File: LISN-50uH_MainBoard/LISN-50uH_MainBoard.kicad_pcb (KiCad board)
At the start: 2 copper layers, 160 x 120 mm, 80 parts, among them J1 Faston Tab 4.8mm, J2 Faston Tab 4.8mm, J3 Faston Tab 4.8mm, J4 Faston Tab 4.8mm, J5 Conn_Coaxial, J6 Conn_Coaxial, J7 Faston Tab 4.8mm, J8 Faston Tab 4.8mm

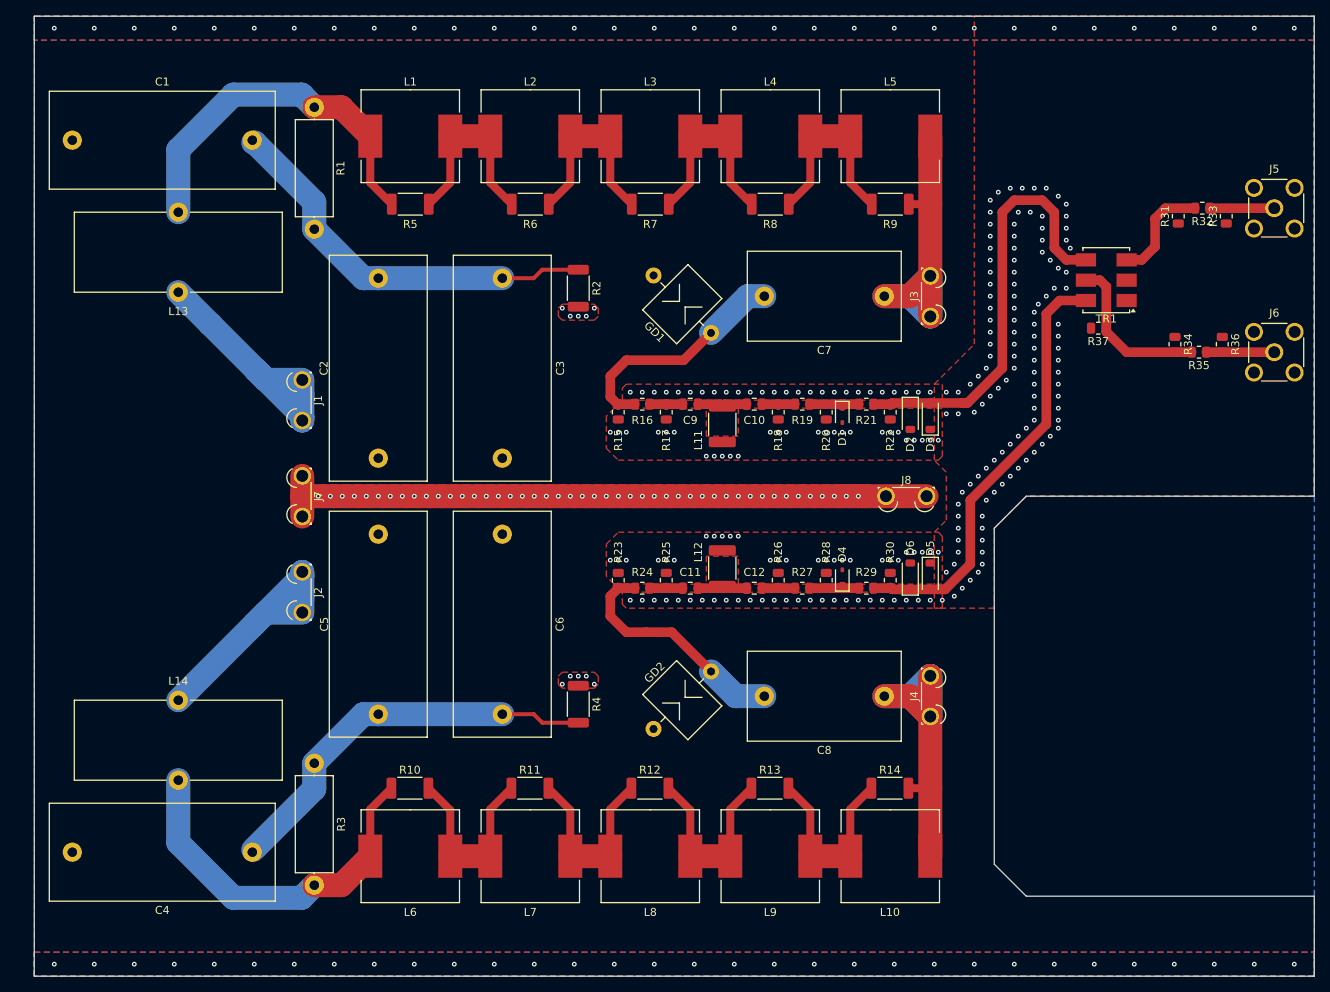
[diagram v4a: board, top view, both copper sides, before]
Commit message: add L&N/CM&DM switch
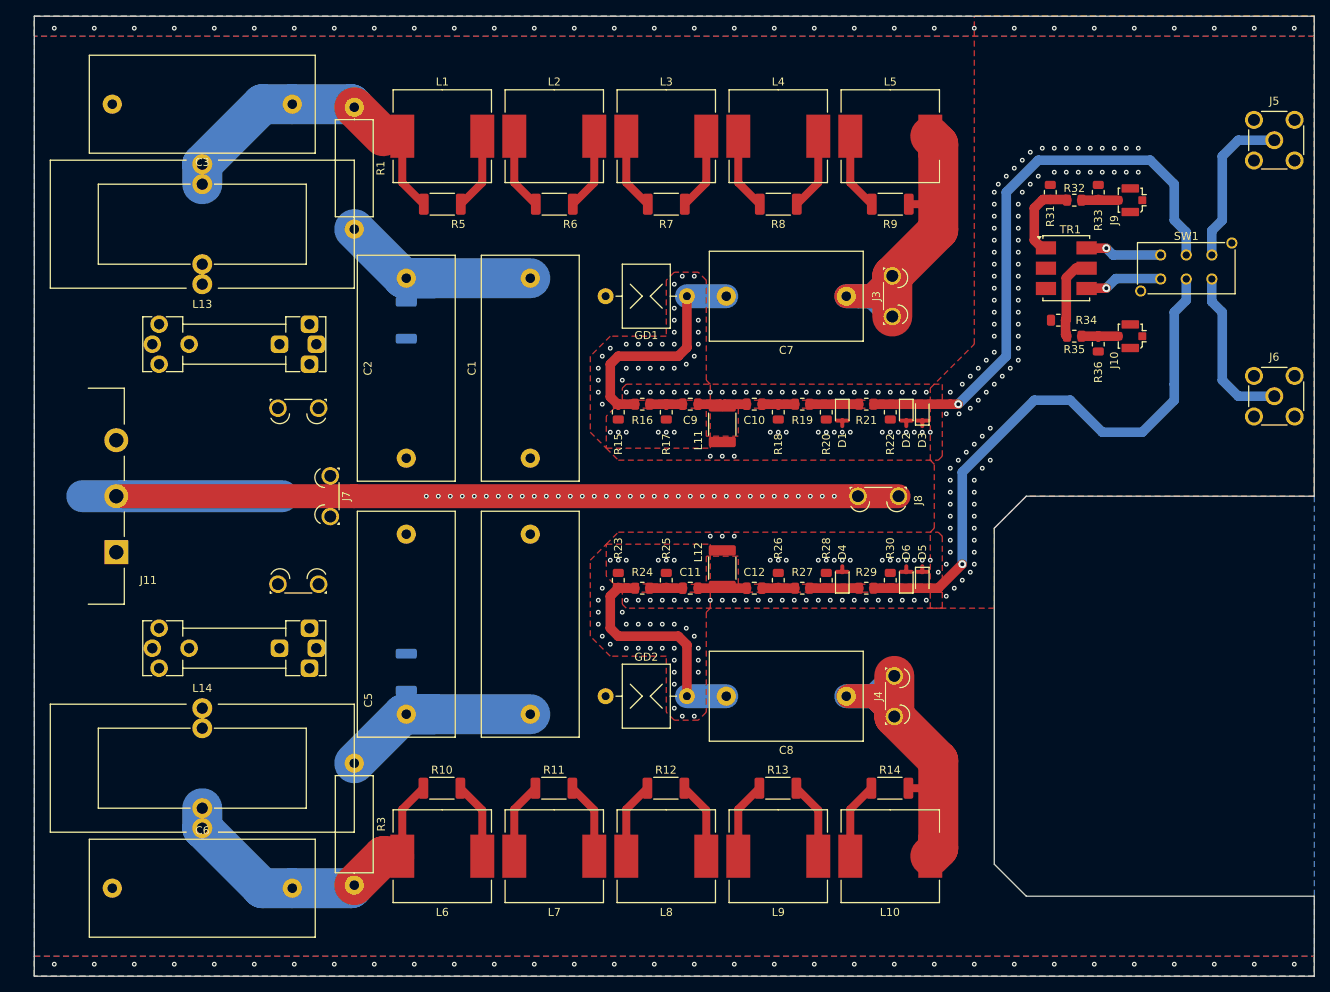
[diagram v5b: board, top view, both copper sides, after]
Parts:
- removed R37: 50R, Resistor_SMD:R_0805_2012Metric
- added F1: 10A, a_project_library:Fuseholder_Clip-5x20mm_Littelfuse_100_111_dual_Horizontal, F.Cu at (95.0, 81.0)
- added F2: 10A, a_project_library:Fuseholder_Clip-5x20mm_Littelfuse_100_111_dual_Horizontal, F.Cu at (95.0, 119.0)
- added J10: Conn_Coaxial, Connector_Coaxial:U.FL_Molex_MCRF_73412-0110_Vertical, F.Cu at (207.0, 80.0)
- added J11: Conn_01x03_Pin, a_project_library:AC_Connector_Adam_tech_IEC-A-4, F.Cu at (80.2, 107.0)
- added J9: Conn_Coaxial, Connector_Coaxial:U.FL_Molex_MCRF_73412-0110_Vertical, F.Cu at (207.0, 63.0)
- added SW1: SW_DPDT_x2, a_project_library:SW_E-SWITCH_LC2255EENP_DPDT_right_angle, F.Cu at (214.0, 71.5)
- D2, D3, D5, D6: value 1N4150 -> BAS321,115; footprint Diode_SMD:D_SOD-123 -> Diode_SMD:D_SOD-323
- L13, L14: footprint a_project_library:L_Toroid_Vertical_L26.0mm_W12.9mm_P10.0mm_Wuerth_WE-FI -> a_project_library:L_Toroid_Vertical_L38.0mm_W16.0mm_P15.0mm_Wuerth_WE-FI
- R2, R4: value R -> 470k; moved to B.Cu
- moved C1 38.8 mm to (132.0, 72.8), turned to -90 degrees
- moved C4 38.8 mm to (132.0, 127.2), turned to 90 degrees
- moved C3 34.1 mm to (102.2, 51.0), turned to 180 degrees
- moved C6 34.1 mm to (102.2, 149.0), turned to 180 degrees
- moved R2 21.9 mm to (116.5, 78.0)
- moved R4 21.9 mm to (116.5, 122.0)
- moved R31 16.3 mm to (197.0, 62.0), turned to -90 degrees
- moved R33 16.3 mm to (203.0, 62.0), turned to -90 degrees
- moved R32 16.0 mm to (200.0, 63.0)
- moved R35 15.7 mm to (200.0, 80.0)
- moved R36 15.5 mm to (203.0, 81.0), turned to 90 degrees
- moved R34 14.9 mm to (198.0, 78.0), turned to 0 degrees
- moved J5 8.50 mm to (225.0, 55.5)
- moved J6 5.50 mm to (225.0, 87.5)
- moved TR1 5.22 mm to (199.0, 71.5), turned to 0 degrees
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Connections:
- C1 pad 1: /L_C -> /L_Cap
- C2 pad 1: /L_C -> /L_Cap
- C3 pad 1: /L_C -> /L_l
- C4 pad 1: /N_C -> /N_Cap
- C5 pad 1: /N_C -> /N_Cap
- C6 pad 1: /N_C -> /N_l
- J5 pad 1: /SIG_DM_out -> Net-(J5-In)
- J6 pad 1: /SIG_CM_out -> Net-(J6-In)
- L13 pad 1: /L_in -> /L_fused
- L14 pad 1: /N_in -> /N_fused
- R1 pad 1: /L_C -> /L_Cap
- R2 pad 2: /L_C -> /L_Cap
- R3 pad 1: /N_C -> /N_Cap
- R4 pad 2: /N_C -> /N_Cap
- TR1 pad 1: GND -> /SIG_DM
- TR1 pad 3: /SIG_DM -> GND
- TR1 pad 4: L_SIG_LIM -> Net-(SW1B-C)
- TR1 pad 6: N_SIG_LIM -> Net-(SW1A-A)
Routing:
- net GND: track 82.1 -> 134.6 mm, vias 344 -> 350
- net /L_C: track 50.1 -> 0.00 mm
- net /N_C: track 50.0 -> 0.00 mm
- net /L_in: track 34.8 -> 0.00 mm
- net /N_in: track 34.6 -> 0.00 mm
- net /N_Cap: track 0.00 -> 31.0 mm
- net /L_Cap: track 0.00 -> 31.0 mm
- net Net-(J6-In): track 0.00 -> 20.5 mm
- net Net-(J5-In): track 0.00 -> 20.2 mm
- net N_SIG_LIM: track 54.4 -> 73.1 mm, vias 0 -> 1
- net L_SIG_LIM: track 54.3 -> 72.9 mm, vias 0 -> 1
- net /SIG_CM: track 20.3 -> 10.4 mm
- net Net-(SW1B-C): track 0.00 -> 9.80 mm, vias 0 -> 1
- net Net-(SW1A-A): track 0.00 -> 9.63 mm, vias 0 -> 1
- net /L_l: track 46.4 -> 39.5 mm
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
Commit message: Planes added
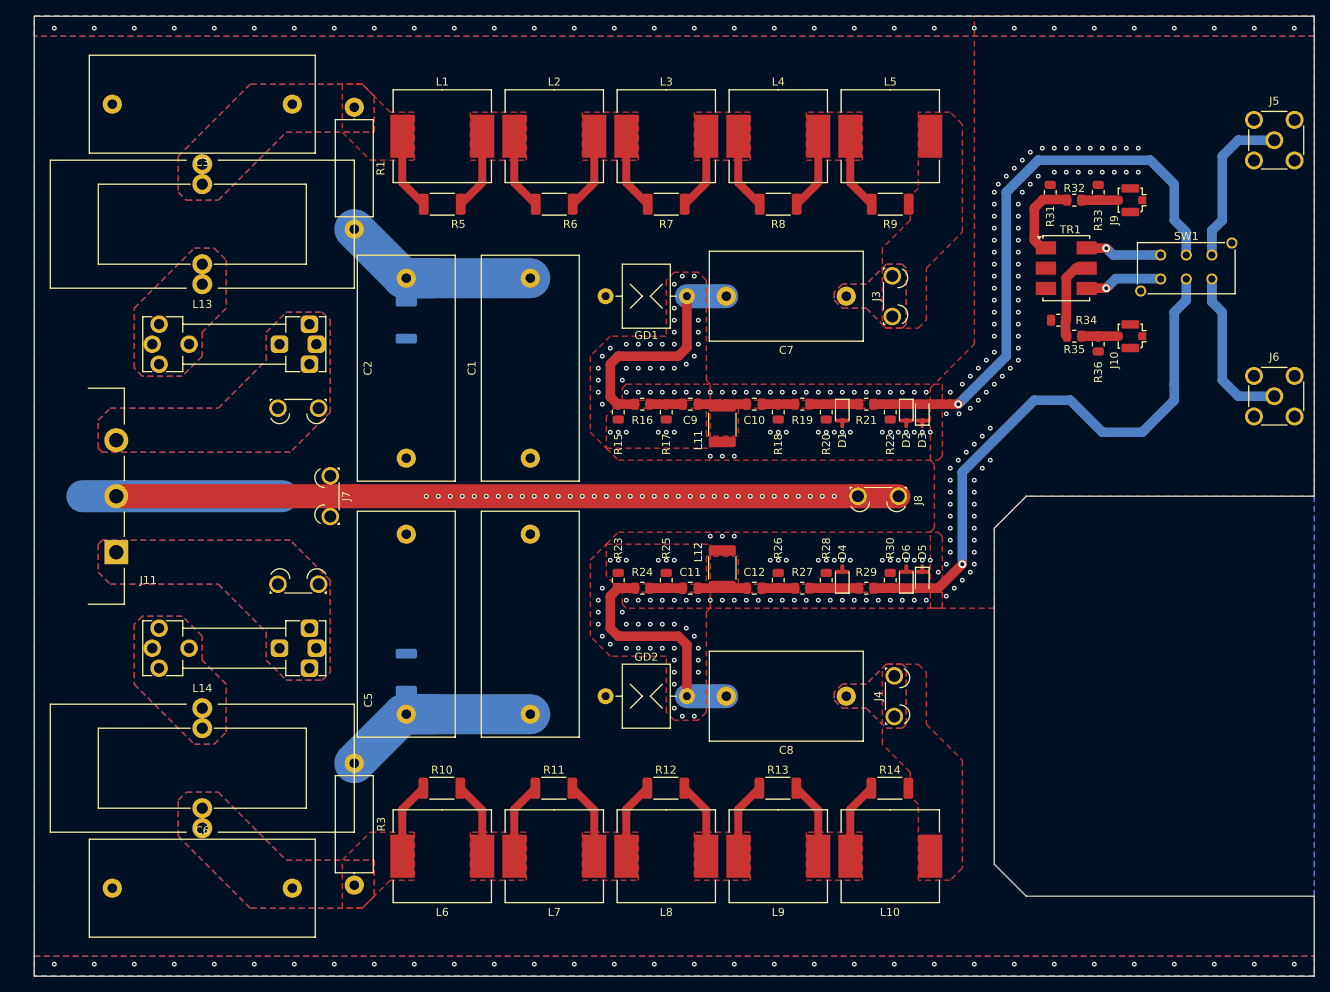
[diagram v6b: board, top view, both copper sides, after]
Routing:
- net /L_dut: track 54.4 -> 0.00 mm
- net /N_dut: track 52.8 -> 0.00 mm
- net /N_l: track 40.9 -> 9.59 mm
- net /L_l: track 39.5 -> 9.61 mm
- added copper zone on B.Cu, net /L_dut
- added copper zone on F.Cu, net /L_dut
- added copper zone on B.Cu, net /L_fused
- added copper zone on F.Cu, net /L_fused
- added copper zone on B.Cu, net /L_in
- added copper zone on F.Cu, net /L_in
- added copper zone on B.Cu, net /L_l
- added copper zone on F.Cu, net /L_l
- added copper zone on F.Cu, net /L_l1
- added copper zone on F.Cu, net /L_l2
- added copper zone on F.Cu, net /L_l3
- added copper zone on F.Cu, net /L_l4
- added copper zone on B.Cu, net /N_dut
- added copper zone on F.Cu, net /N_dut
- added copper zone on B.Cu, net /N_fused
- added copper zone on F.Cu, net /N_fused
- added copper zone on B.Cu, net /N_in
- added copper zone on F.Cu, net /N_in
- added copper zone on B.Cu, net /N_l
- added copper zone on F.Cu, net /N_l
- added copper zone on F.Cu, net /N_l1
- added copper zone on F.Cu, net /N_l2
- added copper zone on F.Cu, net /N_l3
- added copper zone on F.Cu, net /N_l4

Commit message: add RF track via shielding
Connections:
- SW1 pad 7: (no net) -> GND
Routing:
- net GND: vias 350 -> 509

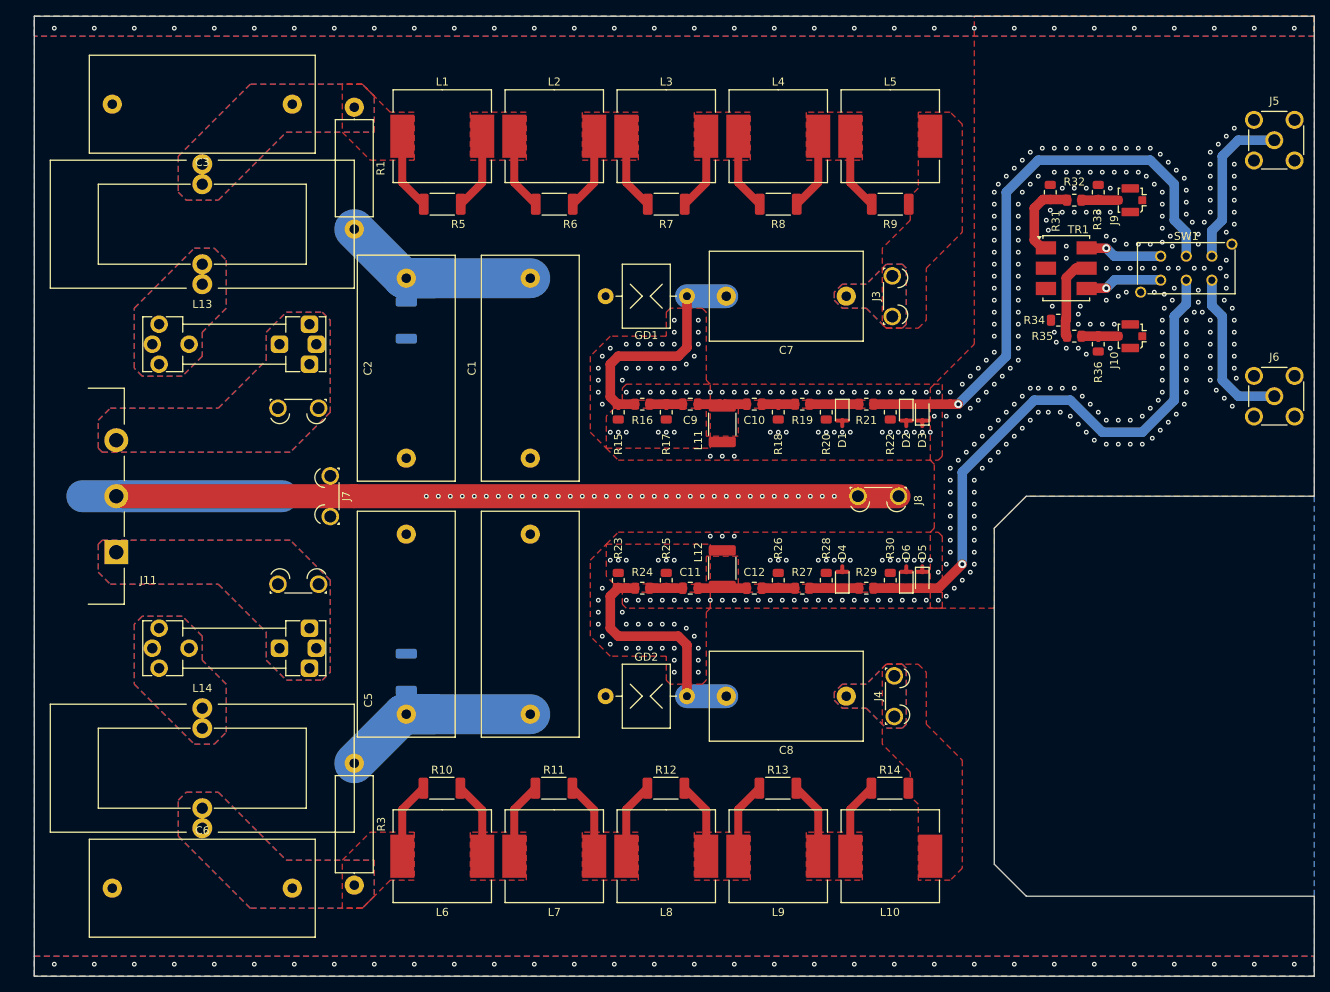
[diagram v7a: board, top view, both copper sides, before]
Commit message: move CM DM to dedicated PCB
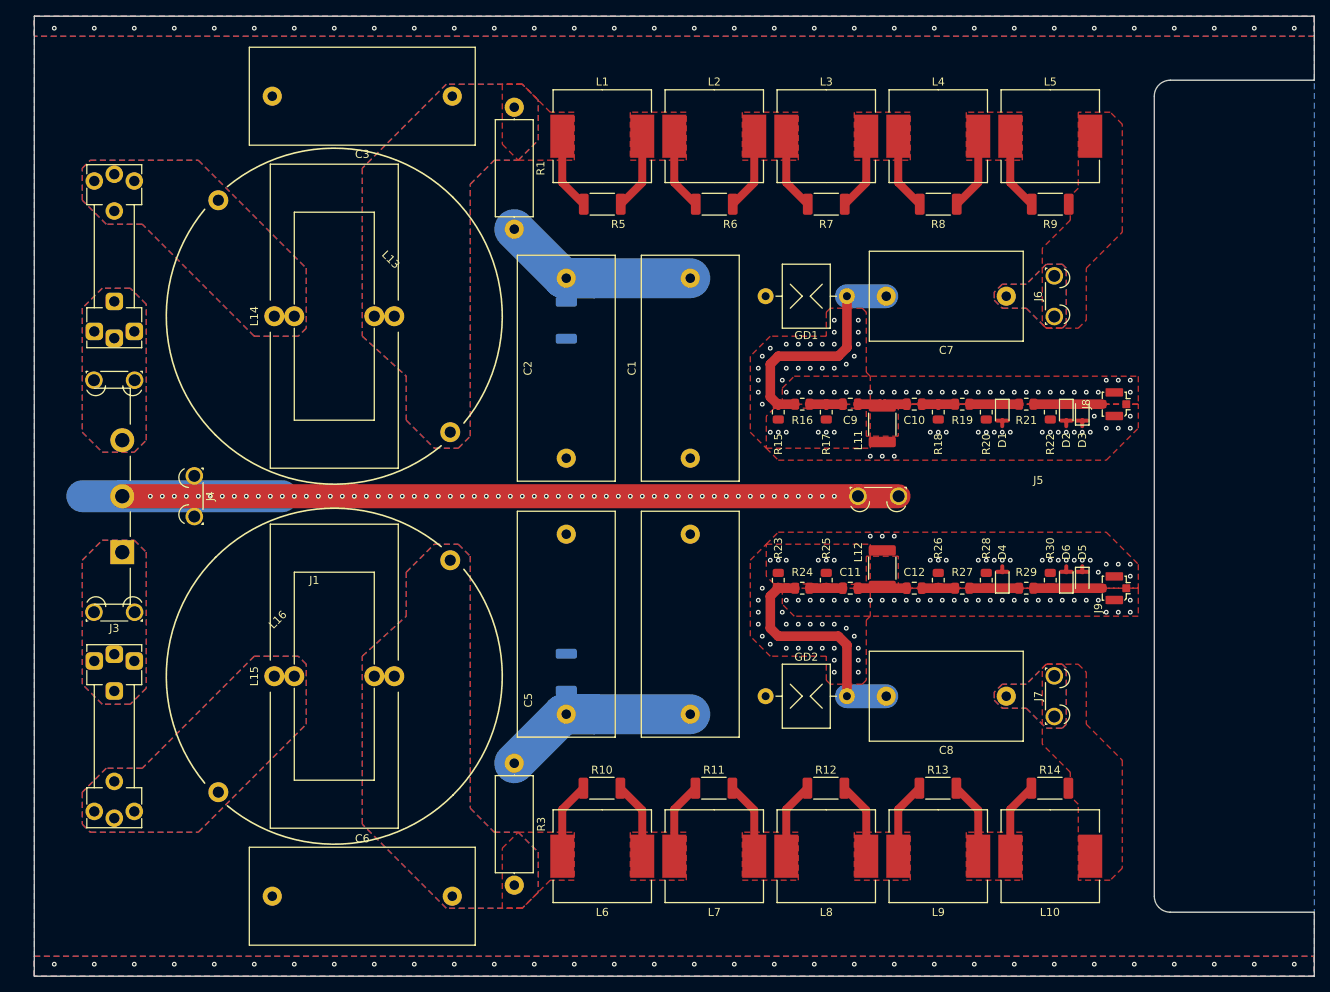
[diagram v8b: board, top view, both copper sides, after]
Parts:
- removed J10: Conn_Coaxial, Connector_Coaxial:U.FL_Molex_MCRF_73412-0110_Vertical
- removed J11: Conn_01x03_Pin, a_project_library:AC_Connector_Adam_tech_IEC-A-4
- removed R31, R33, R34, R36: DNP, Resistor_SMD:R_0805_2012Metric
- removed R32: 0, Resistor_SMD:R_0805_2012Metric
- removed R35: 0R, Resistor_SMD:R_0805_2012Metric
- removed SW1: SW_DPDT_x2, a_project_library:SW_E-SWITCH_LC2255EENP_DPDT_right_angle
- removed TR1: ADT1-6T, RF_Mini-Circuits:Mini-Circuits_CD637_H5.23mm
- added L15: 250uH optional, a_project_library:L_Toroid_Vertical_L38.0mm_W16.0mm_P15.0mm_Wuerth_WE-FI, F.Cu at (107.5, 122.5)
- added L16: 250uH optional, a_project_library:L_Toroid_Horizontal_D42.0mm_H21.5mm_Abracon_ATCA-08, F.Cu at (107.5, 122.5)
- J1: value Faston Tab 4.8mm -> Conn_01x03_Pin; footprint a_project_library:Faston_Tab_4.8x0.8 -> a_project_library:AC_Connector_Adam_tech_IEC-A-4
- J5, J6: value Conn_Coaxial -> Faston Tab 4.8mm; footprint Connector_Coaxial:SMA_Molex_73251-2200_Horizontal -> a_project_library:Faston_Tab_4.8x0.8
- J8: value Faston Tab 4.8mm -> Conn_Coaxial; footprint a_project_library:Faston_Tab_4.8x0.8 -> Connector_Coaxial:U.FL_Molex_MCRF_73412-0110_Vertical
- L13: footprint a_project_library:L_Toroid_Vertical_L38.0mm_W16.0mm_P15.0mm_Wuerth_WE-FI -> a_project_library:L_Toroid_Horizontal_D42.0mm_H21.5mm_Abracon_ATCA-08
- moved J3 105.0 mm to (80.0, 114.5), turned to 0 degrees
- moved J7 93.9 mm to (197.5, 125.0), turned to -90 degrees
- moved J4 91.0 mm to (90.0, 100.0), turned to 90 degrees
- moved J5 66.6 mm to (175.5, 100.0), turned to 180 degrees
- moved L14 58.9 mm to (107.5, 77.5), turned to 90 degrees
- moved J9 48.5 mm to (205.0, 111.5)
- moved J2 34.3 mm to (80.0, 85.5), turned to 180 degrees
- moved J8 31.7 mm to (205.0, 88.5), turned to -90 degrees
- moved J6 30.2 mm to (197.5, 75.0)
- moved J1 28.4 mm to (81.0, 107.0)
- moved L13 20.1 mm to (107.5, 77.5), turned to -45 degrees
- moved C3 20.0 mm to (122.2, 50.0)
- moved C6 20.0 mm to (122.2, 150.0)
- moved C1 20.0 mm to (152.0, 72.8)
- moved C10 20.0 mm to (180.0, 88.5)
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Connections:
- D2 pad 2: L_SIG_LIM -> /L_SIG_LIM
- D3 pad 1: L_SIG_LIM -> /L_SIG_LIM
- D5 pad 2: N_SIG_LIM -> /N_SIG_LIM
- D6 pad 1: N_SIG_LIM -> /N_SIG_LIM
- J1 pad 1: /L_in -> /N_in
- J2 pad 1: /N_in -> /L_in
- J3 pad 1: /L_dut -> /N_in
- J4 pad 1: /N_dut -> GND
- J5 pad 1: Net-(J5-In) -> GND
- J6 pad 1: Net-(J6-In) -> /L_dut
- J7 pad 1: GND -> /N_dut
- J8 pad 1: GND -> /L_SIG_LIM
- J9 pad 1: /SIG_DM_out -> /N_SIG_LIM
- L14 pad 1: /N_fused -> /L_fused
- L14 pad 2: /N_l -> /L_l
- R21 pad 1: L_SIG_LIM -> /L_SIG_LIM
- R22 pad 2: L_SIG_LIM -> /L_SIG_LIM
- R29 pad 1: N_SIG_LIM -> /N_SIG_LIM
- R30 pad 2: N_SIG_LIM -> /N_SIG_LIM
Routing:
- net L_SIG_LIM: track 73.1 -> 0.00 mm, vias 1 -> 0
- net N_SIG_LIM: track 73.0 -> 0.00 mm, vias 1 -> 0
- net Net-(J6-In): track 20.4 -> 0.00 mm
- net Net-(J5-In): track 20.4 -> 0.00 mm
- net /SIG_CM: track 10.4 -> 0.00 mm
- net /SIG_DM: track 10.4 -> 0.00 mm
- net Net-(SW1B-C): track 9.73 -> 0.00 mm, vias 1 -> 0
- net Net-(SW1A-A): track 9.69 -> 0.00 mm, vias 1 -> 0
- net /N_SIG_LIM: track 0.00 -> 8.59 mm
- net /L_SIG_LIM: track 0.00 -> 8.59 mm
- net /SIG_CM_out: track 4.66 -> 0.00 mm
- net /SIG_DM_out: track 4.66 -> 0.00 mm
- net GND: vias 509 -> 290
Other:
- outline, holes or cut-outs redrawn
